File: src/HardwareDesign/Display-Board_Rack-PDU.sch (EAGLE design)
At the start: 46 parts, among them IC1 MCP23S18-E/MJ

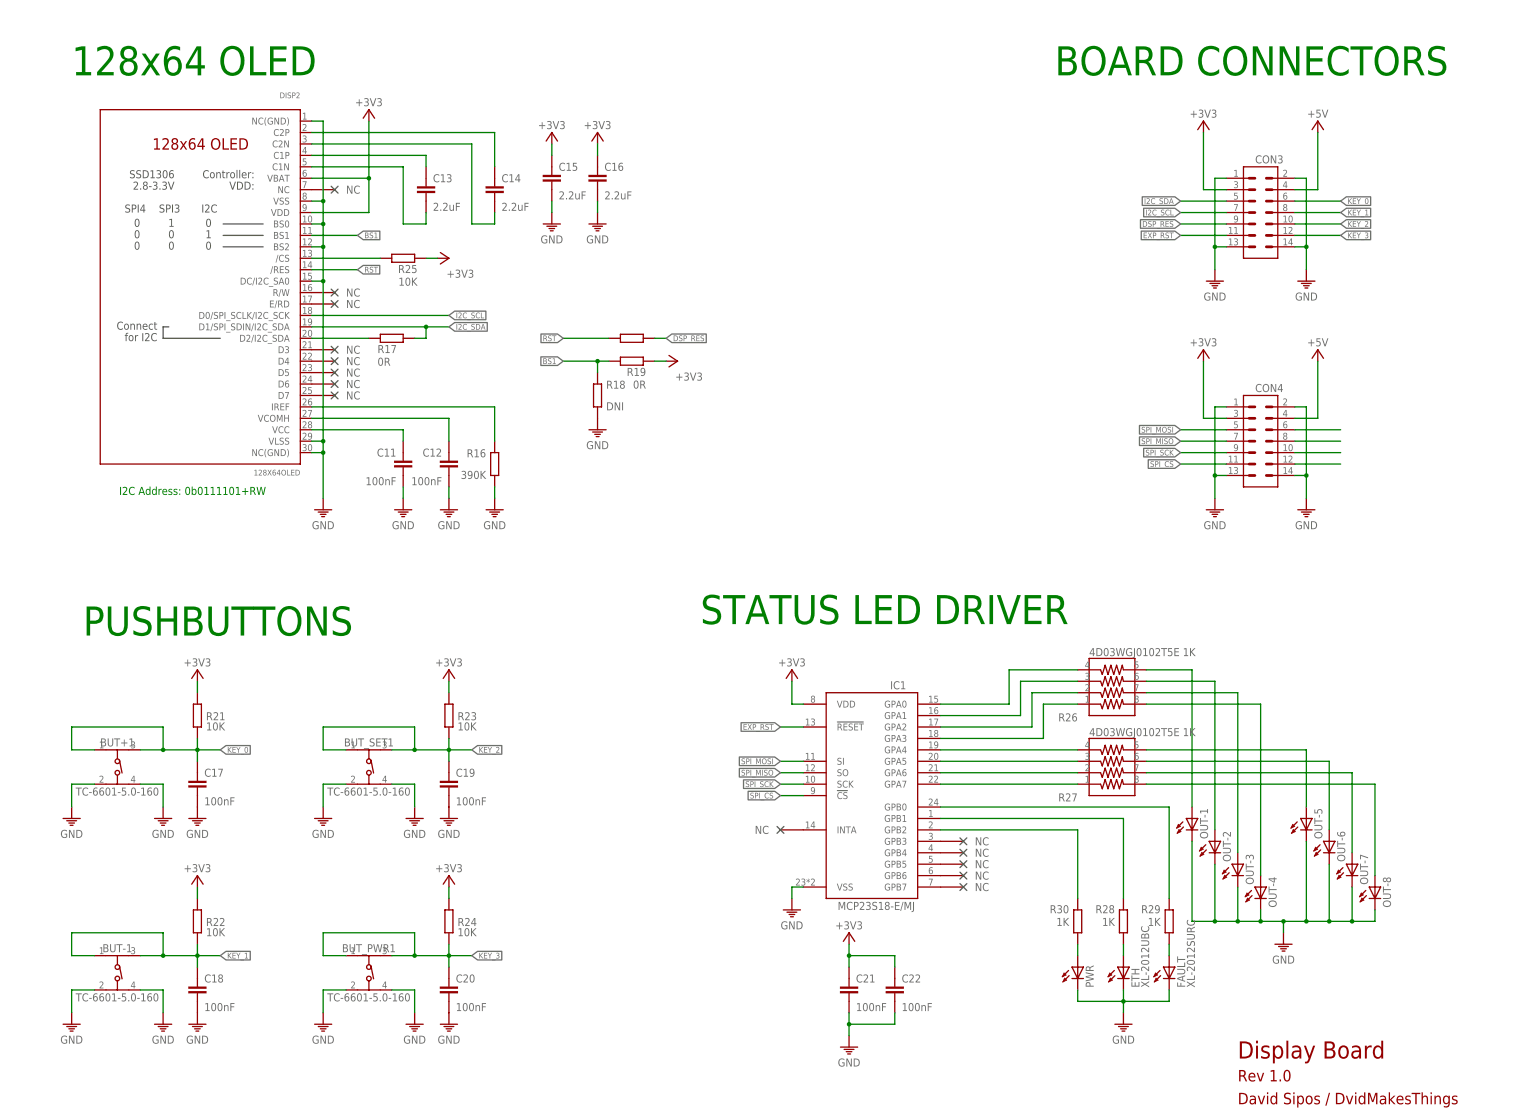
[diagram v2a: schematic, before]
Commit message: start Displayboard rev 2
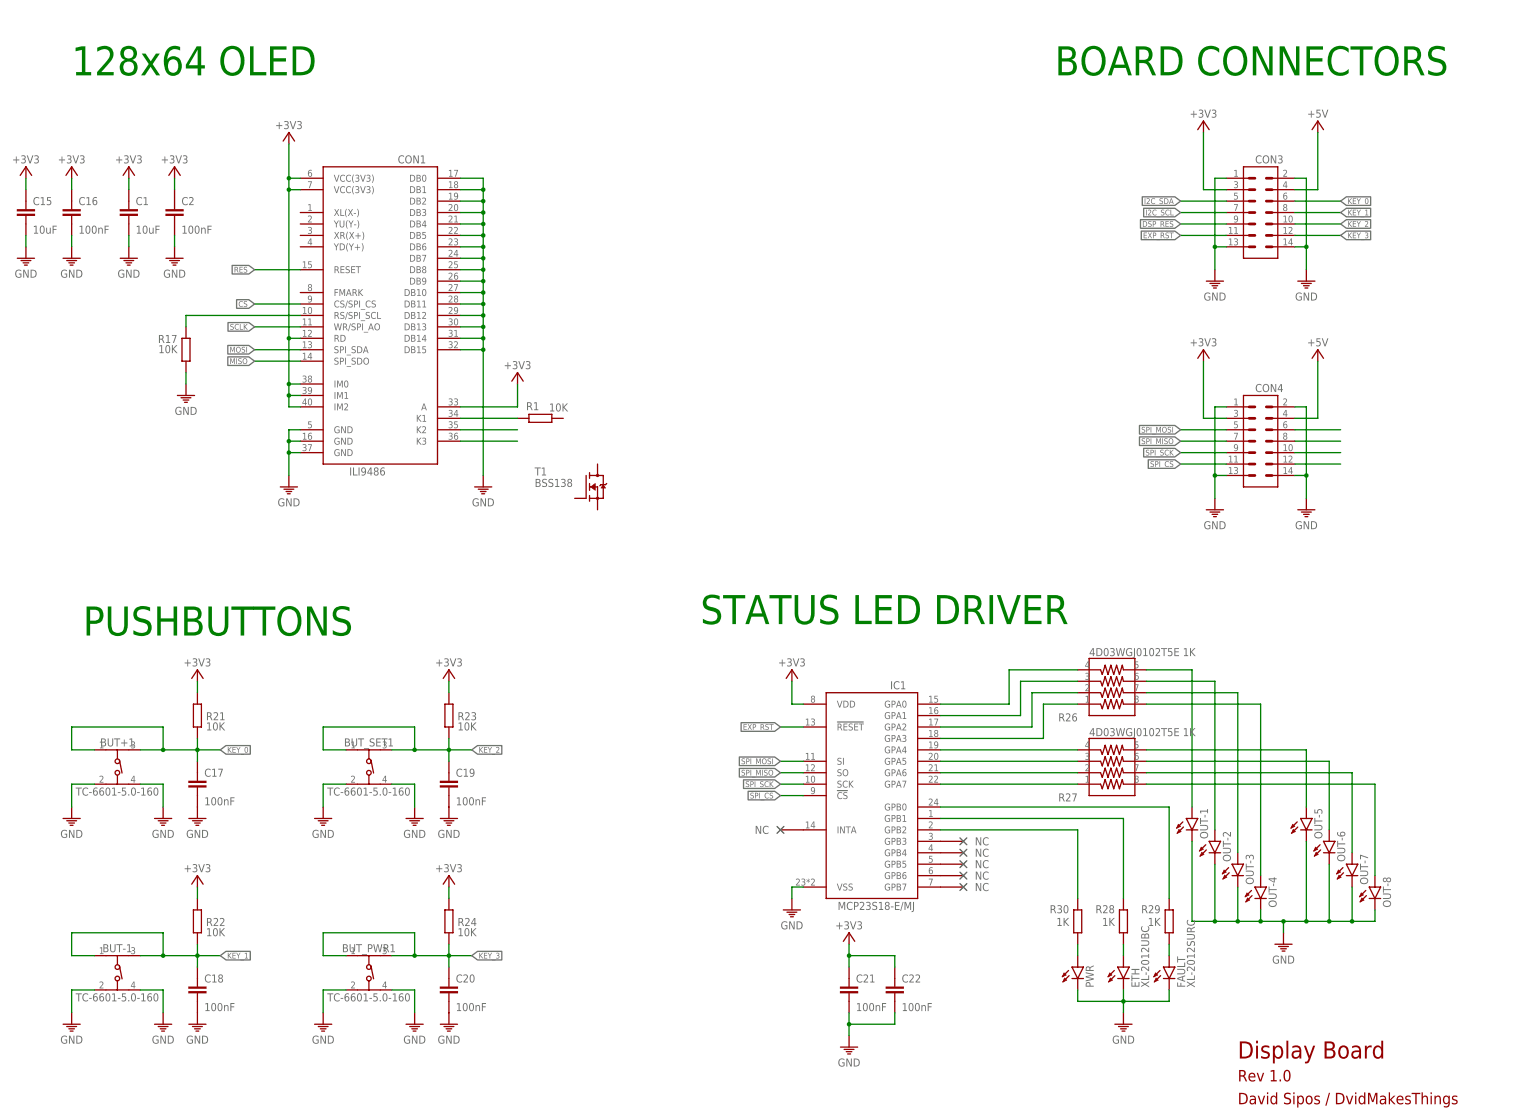
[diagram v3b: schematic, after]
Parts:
- removed C11, C12: 100nF, ds_passive:C0402
- removed C13, C14: 2.2uF, ds_passive:C0402
- removed DISP2: 128X64OLED, ds_displays:128X64OLED
- removed R16: 390K, ds_passive:R0402
- removed R18: DNI, ds_passive:R0402
- removed R19, R20: 0R, ds_passive:R0402
- removed R25: 10K, ds_passive:R0402
- added C1: 10uF, ds_passive:C-0402
- added C2: 100nF, ds_passive:C-0402
- added CON1: 3.5IN_TFTLCD, ds_displays:3.5IN_TFTLCD
- added R1: 10K, ds_passive:R0402
- added T1: BSS138, transistor-fet:BSS138
- C15: value 2.2uF -> 10uF; device ds_passive:C0402 -> ds_passive:C-0402
- C16: value 2.2uF -> 100nF; device ds_passive:C0402 -> ds_passive:C-0402
- C17, C18, C19, C20, C21, C22: device ds_passive:C0402 -> ds_passive:C-0402
- R17: value 0R -> 10K
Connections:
- removed net BS1: DISP2.BS1, R18.1, R19.2
- removed net N$22: C13.2, DISP2.C1N
- removed net N$35: C13.1, DISP2.C1P
- removed net N$36: C14.2, DISP2.C2N
- removed net N$37: C14.1, DISP2.C2P
- removed net N$38: DISP2.IREF, R16.1
- removed net N$39: C11.1, DISP2.VCC
- removed net N$40: C12.1, DISP2.VCOMH
- removed net N$41: DISP2.D2/I2C_SDA, R17.1
- removed net N$49: DISP2./CS, R25.2
- removed net RST: DISP2./RES, R20.1
- new net CS: CON1.CS/SPI_CS
- new net MISO: CON1.SPI_SDO
- new net MOSI: CON1.SPI_SDA
- new net N$1: CON1.RS/SPI_SCL, R17.2
- new net N$2: CON1.K2
- new net N$3: CON1.K3
- new net N$5: CON1.K1, R1.2
- new net RES: CON1.RESET
- new net SCLK: CON1.WR/SPI_AO
- net +3V3: now also C1.1, C2.1, CON1.A, CON1.IM0, CON1.IM1, CON1.IM2, CON1.RD, CON1.VCC(3V3)@1, CON1.VCC(3V3)@2; no longer DISP2.VBAT, DISP2.VDD, R19.1, R25.1
- net DSP_RES: no longer R20.2
- net GND: now also C1.2, C2.2, CON1.DB0, CON1.DB1, CON1.DB10, CON1.DB11, CON1.DB12, CON1.DB13, CON1.DB14, CON1.DB15, CON1.DB2, CON1.DB3, CON1.DB4, CON1.DB5, CON1.DB6, CON1.DB7, CON1.DB8, CON1.DB9, CON1.GND@1, CON1.GND@2, CON1.GND@3, R17.1; no longer C11.2, C12.2, DISP2.BS0, DISP2.BS2, DISP2.DC/I2C_SA0, DISP2.NC(GND)@1, DISP2.NC(GND)@2, DISP2.VLSS, DISP2.VSS, R16.2, R18.2
- net I2C_SCL: no longer DISP2.D0/SPI_SCLK/I2C_SCK
- net I2C_SDA: no longer DISP2.D1/SPI_SDIN/I2C_SDA, R17.2
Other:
- note removed: "I2C Address: 0b0111101+RW"
- moved on the sheet: C15, C16, R17
